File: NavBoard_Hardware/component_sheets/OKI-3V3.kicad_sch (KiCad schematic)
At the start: 4 parts

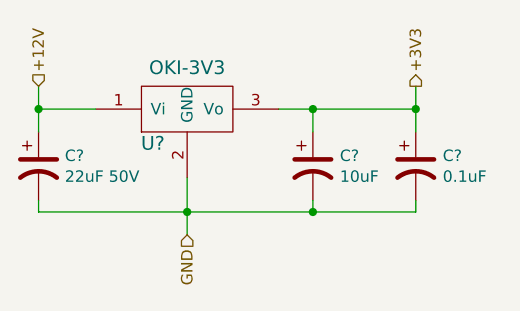
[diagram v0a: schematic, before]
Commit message: Created adapter symbols and footprints
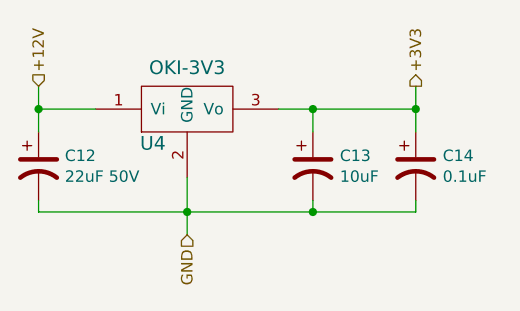
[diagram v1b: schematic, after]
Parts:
- gave numbers to parts that had none: 4
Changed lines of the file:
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@@
   (symbol (lib_id "MRDT_Devices:OKI") (at 220.98 148.59 0) (unit 1)
     (in_bom yes) (on_board yes)
-    (property "Reference" "U?" (id 0) (at 222.25 149.86 0)
+    (property "Reference" "U4" (id 0) (at 222.25 149.86 0)
       (effects (font (size 1.524 1.524)))
     )
@@
   (symbol (lib_id "Device:C_Polarized_US") (at 209.55 152.4 0) (unit 1)
     (in_bom yes) (on_board yes)
-    (property "Reference" "C?" (id 0) (at 212.471 151.2316 0)
+    (property "Reference" "C12" (id 0) (at 212.471 151.2316 0)
       (effects (font (size 1.27 1.27)) (justify left))
     )
@@
   (symbol (lib_id "Device:C_Polarized_US") (at 251.46 152.4 0) (unit 1)
     (in_bom yes) (on_board yes)
-    (property "Reference" "C?" (id 0) (at 254.4572 151.2316 0)
+    (property "Reference" "C14" (id 0) (at 254.4572 151.2316 0)
       (effects (font (size 1.27 1.27)) (justify left))
     )
@@
   (symbol (lib_id "Device:C_Polarized_US") (at 240.03 152.4 0) (unit 1)
     (in_bom yes) (on_board yes)
-    (property "Reference" "C?" (id 0) (at 243.0272 151.2316 0)
+    (property "Reference" "C13" (id 0) (at 243.0272 151.2316 0)
       (effects (font (size 1.27 1.27)) (justify left))
     )

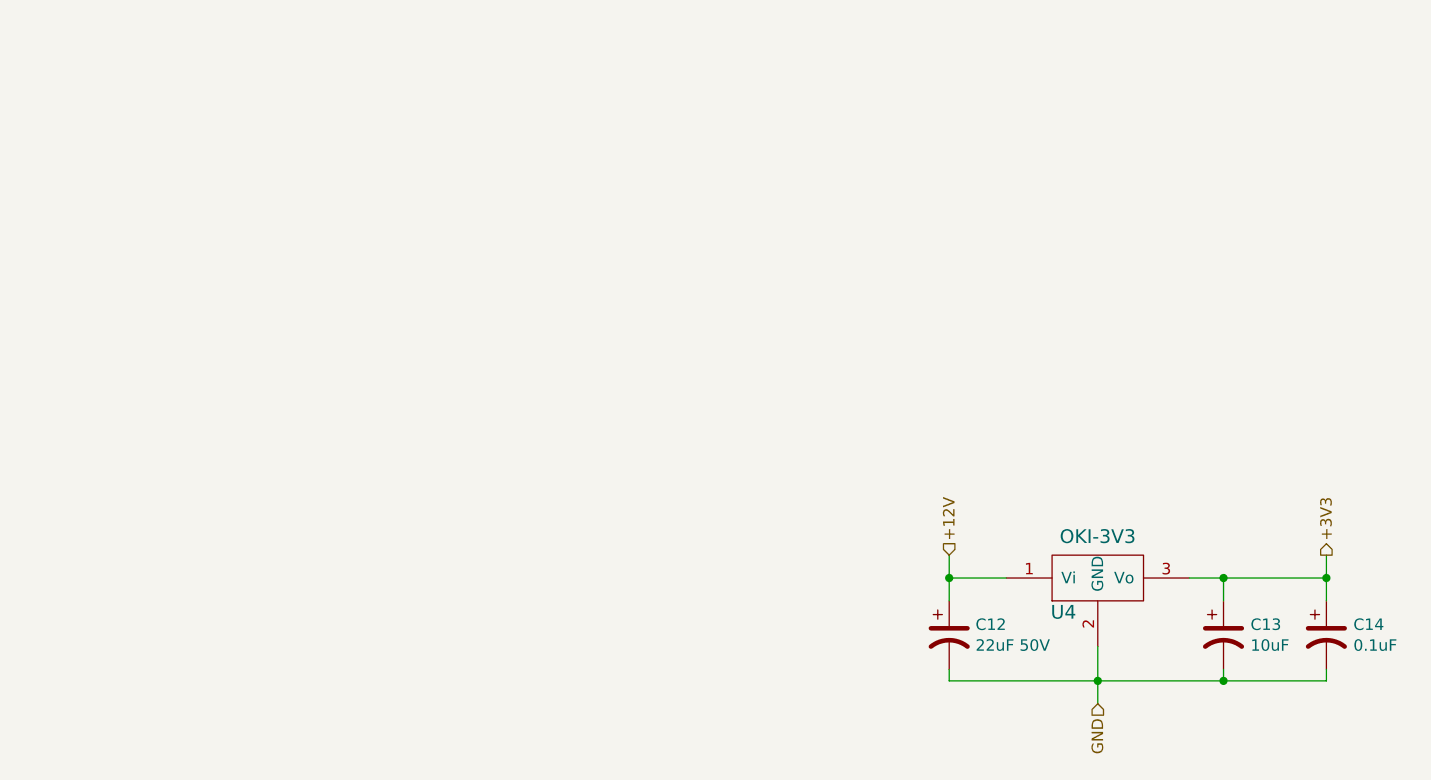
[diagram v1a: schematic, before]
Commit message: Added connectors, cleaned up file directory
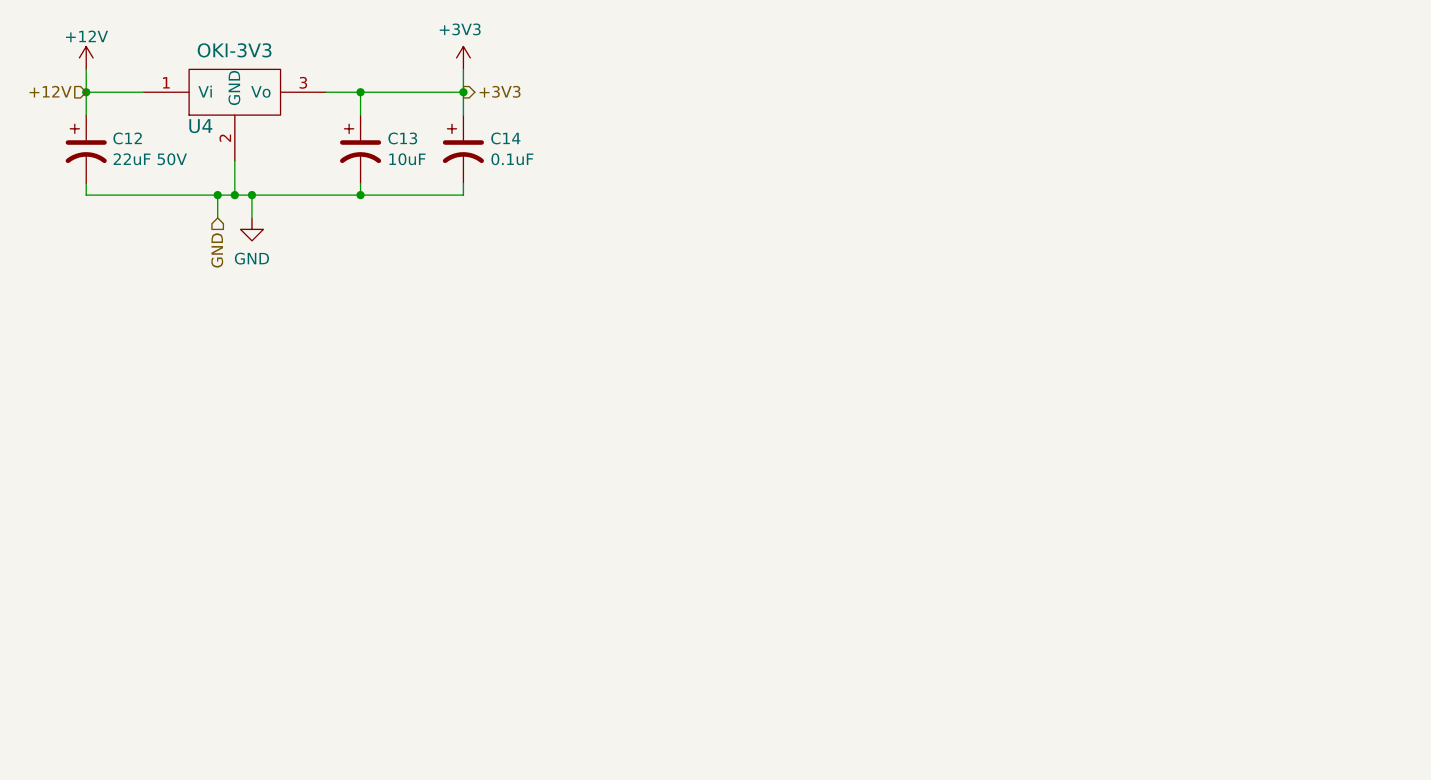
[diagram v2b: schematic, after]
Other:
- moved on the sheet: C12, C13, C14, U4

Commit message: Placed OKI SMD components, aligned ethernet pins
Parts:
- C12: footprint Capacitor_THT:CP_Radial_D6.3mm_P2.50mm -> Capacitor_SMD:C_1206_3216Metric_Pad1.33x1.80mm_HandSolder
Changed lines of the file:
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@@
       (effects (font (size 1.27 1.27)) (justify left))
     )
-    (property "Footprint" "Capacitor_THT:CP_Radial_D6.3mm_P2.50mm" (id 2) (at 113.665 98.425 0)
+    (property "Footprint" "Capacitor_SMD:C_1206_3216Metric_Pad1.33x1.80mm_HandSolder" (id 2) (at 113.665 98.425 0)
       (effects (font (size 1.27 1.27)) hide)
     )

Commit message: Annotated schematic pages
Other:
- company: Missouri S&T Mars Rover Design Team -> Thomas Francois, Missouri S&T Mars Rover Design Team
- title: OKI 3V3 Voltage Regulator -> MRDT NavBoard - OKI 3V3 Voltage Regulator
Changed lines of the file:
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@@
   (paper "A4")
   (title_block
-    (title "OKI 3V3 Voltage Regulator")
+    (title "MRDT NavBoard - OKI 3V3 Voltage Regulator")
     (date "2022-09-17")
-    (rev "2, 2023")
-    (company "Missouri S&T Mars Rover Design Team")
+    (rev "1, 2023")
+    (company "Thomas Francois, Missouri S&T Mars Rover Design Team")
     (comment 1 "OKI 3V3 Voltage Regulator")
-    (comment 2 "Provides Stable 3V3 From 12V")
+    (comment 2 "Provides stable 3V3 from 12V input")
   )
   (junction (at 113.665 92.075) (diameter 0) (color 0 0 0 0)
